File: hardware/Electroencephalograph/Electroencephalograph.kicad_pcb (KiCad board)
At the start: 2 copper layers, 89 parts, among them U1 ADS1298IPAG, U2 OPA330xxD

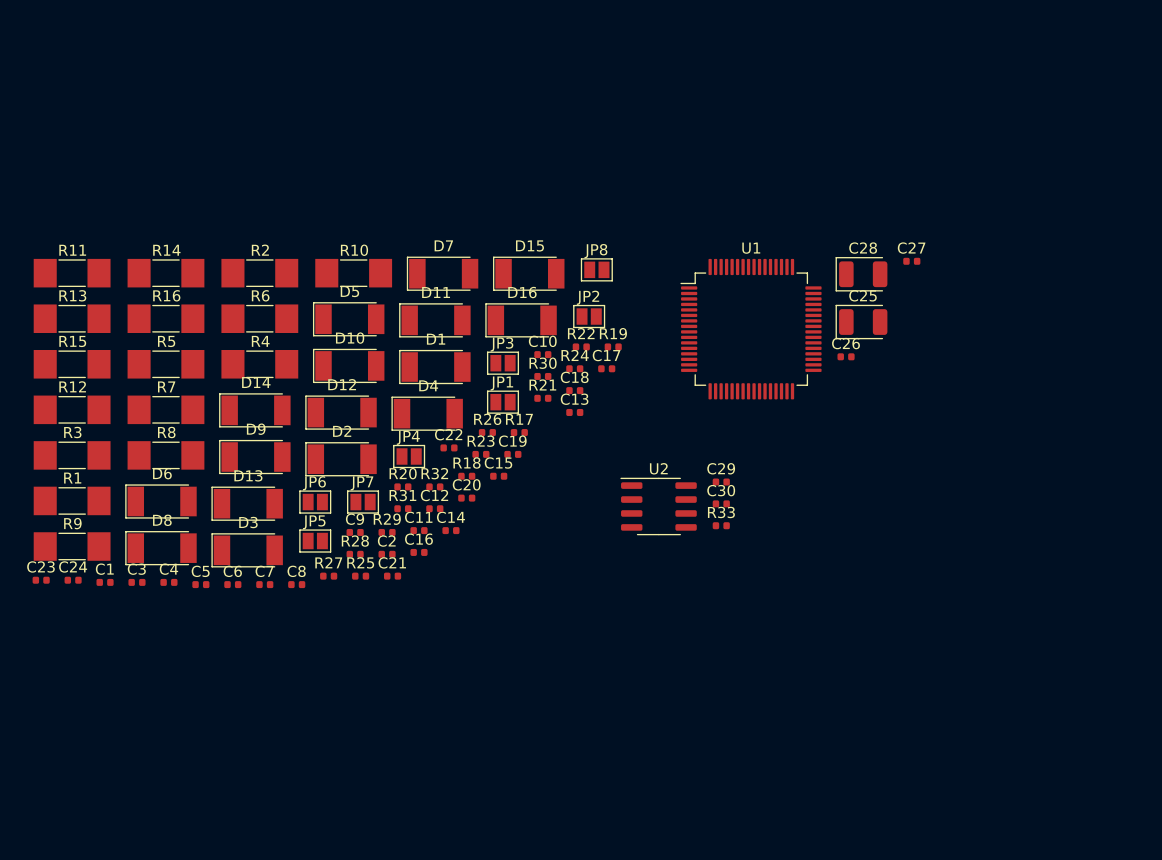
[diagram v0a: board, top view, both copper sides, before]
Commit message: paritial routing for analog part
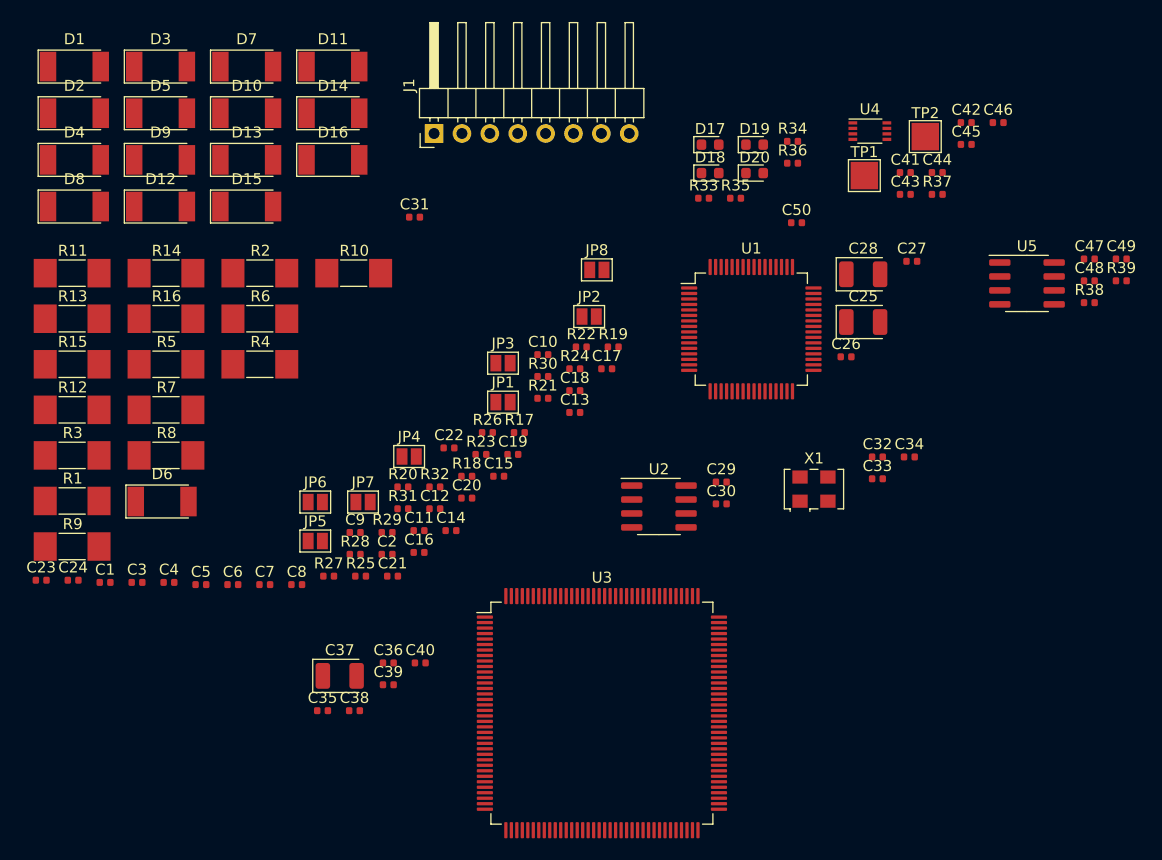
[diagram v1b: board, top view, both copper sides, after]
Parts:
- added C31: 1n, Capacitor_SMD:C_0402_1005Metric, F.Cu at (163.8, 45.0)
- added C32: 1u, Capacitor_SMD:C_0402_1005Metric, F.Cu at (206.0, 66.8)
- added C33: 1u, Capacitor_SMD:C_0402_1005Metric, F.Cu at (206.0, 68.8)
- added C34: 1u, Capacitor_SMD:C_0402_1005Metric, F.Cu at (208.9, 66.8)
- added C35: 100n, Capacitor_SMD:C_0402_1005Metric, F.Cu at (155.4, 89.9)
- added C36: 100n, Capacitor_SMD:C_0402_1005Metric, F.Cu at (161.4, 85.6)
- added C37: 10u, Capacitor_Tantalum_SMD:CP_EIA-3528-21_Kemet-B, F.Cu at (157.0, 86.7)
- added C38: 100n, Capacitor_SMD:C_0402_1005Metric, F.Cu at (158.4, 89.9)
- added C39: 1u, Capacitor_SMD:C_0402_1005Metric, F.Cu at (161.4, 87.6)
- added C40: 1u, Capacitor_SMD:C_0402_1005Metric, F.Cu at (164.3, 85.6)
- added C41: 1u, Capacitor_SMD:C_0402_1005Metric, F.Cu at (208.5, 40.9)
- added C42: 100n, Capacitor_SMD:C_0402_1005Metric, F.Cu at (214.1, 36.3)
- added C43: 100n, Capacitor_SMD:C_0402_1005Metric, F.Cu at (208.5, 42.9)
- added C44: 1u, Capacitor_SMD:C_0402_1005Metric, F.Cu at (211.4, 40.9)
- added C45: 10u, Capacitor_SMD:C_0402_1005Metric, F.Cu at (214.1, 38.3)
- added C46: 100u, Capacitor_SMD:C_0402_1005Metric, F.Cu at (217.0, 36.3)
- added C47: 100n, Capacitor_SMD:C_0402_1005Metric, F.Cu at (225.3, 48.8)
- added C48: 22n, Capacitor_SMD:C_0402_1005Metric, F.Cu at (225.3, 50.8)
- added C49: 100n, Capacitor_SMD:C_0402_1005Metric, F.Cu at (228.2, 48.8)
- added C50: 100n, Capacitor_SMD:C_0402_1005Metric, F.Cu at (198.6, 45.5)
- added D17: LED, LED_SMD:LED_0603_1608Metric, F.Cu at (190.8, 38.4)
- added D18: LED, LED_SMD:LED_0603_1608Metric, F.Cu at (190.8, 40.9)
- added D19: LED, LED_SMD:LED_0603_1608Metric, F.Cu at (194.8, 38.4)
- added D20: LED, LED_SMD:LED_0603_1608Metric, F.Cu at (194.8, 40.9)
- added J1: Conn_01x08_Male, Connector_PinHeader_2.54mm:PinHeader_1x08_P2.54mm_Horizontal, F.Cu at (165.6, 37.3)
- added R34: 220R, Resistor_SMD:R_0402_1005Metric, F.Cu at (198.3, 38.1)
- added R35: 220R, Resistor_SMD:R_0402_1005Metric, F.Cu at (193.1, 43.2)
- added R36: 220R, Resistor_SMD:R_0402_1005Metric, F.Cu at (198.3, 40.0)
- added R37: 100R, Resistor_SMD:R_0402_1005Metric, F.Cu at (211.4, 42.9)
- added R38: 10R, Resistor_SMD:R_0402_1005Metric, F.Cu at (225.3, 52.7)
- added R39: 100k, Resistor_SMD:R_0402_1005Metric, F.Cu at (228.2, 50.8)
- added TP1: TestPoint_Alt, TestPoint:TestPoint_Pad_2.5x2.5mm, F.Cu at (204.8, 41.2)
- added TP2: TestPoint_Alt, TestPoint:TestPoint_Pad_2.5x2.5mm, F.Cu at (210.4, 37.6)
- added U3: TMS320LF2406PZ, Package_QFP:LQFP-144_20x20mm_P0.5mm, F.Cu at (180.9, 90.1)
- added U4: REF5025, Package_SO:VSSOP-8_2.3x2mm_P0.5mm, F.Cu at (205.3, 37.1)
- added U5: OPA350, Package_SO:SOIC-8_3.9x4.9mm_P1.27mm, F.Cu at (219.6, 51.0)
- added X1: 2M048, Oscillator:Oscillator_SMD_EuroQuartz_XO53-4Pin_5.0x3.2mm, F.Cu at (200.2, 69.7)
- C25: value 1u -> 22u
- R33: value not mounted -> 220R
- moved D3 44.8 mm to (140.7, 31.2)
- moved D1 42.8 mm to (132.8, 31.2)
- moved D2 39.9 mm to (132.8, 35.5)
- moved D4 39.7 mm to (132.8, 39.7)
- moved D8 32.1 mm to (132.8, 44.0)
- moved D13 31.3 mm to (148.5, 39.7)
- moved R33 29.9 mm to (190.2, 43.2)
- moved D9 28.4 mm to (140.7, 39.7)
- moved D14 28.0 mm to (156.4, 35.5)
- moved D15 26.5 mm to (148.5, 44.0)
- moved D7 26.0 mm to (148.5, 31.2)
- moved D5 25.5 mm to (140.7, 35.5)
- moved D12 25.0 mm to (140.7, 44.0)
- moved D11 25.0 mm to (156.4, 31.2)
- moved D10 24.9 mm to (148.5, 35.5)
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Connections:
- C1 pad 1: Net-(C1-Pad1) -> ECC_1
- C2 pad 1: Net-(C2-Pad1) -> ECC_2
- C21 pad 1: Net-(C21-Pad1) -> ECC_6
- C22 pad 1: Net-(C22-Pad1) -> ECC_5
- C23 pad 1: Net-(C23-Pad1) -> ECC_8
- C24 pad 1: Net-(C24-Pad1) -> ECC_7
- C25 pad 2: GNDA -> VDDA
- C26 pad 1: Net-(C25-Pad1) -> Net-(C26-Pad1)
- C26 pad 2: GNDA -> VDDA
- C27 pad 1: Net-(C27-Pad1) -> VDDA
- C28 pad 1: Net-(C27-Pad1) -> VDDA
- C3 pad 1: Net-(C3-Pad1) -> ECC_4
- C4 pad 1: Net-(C4-Pad1) -> ECC_3
- D1 pad 1: Net-(C1-Pad2) -> VDDA
- D1 pad 2: VDDA -> Net-(C1-Pad2)
- D12 pad 1: VDDA -> Net-(C14-Pad1)
- D12 pad 2: Net-(C16-Pad1) -> VDDA
- D13 pad 1: Net-(C18-Pad1) -> VDDA
- D13 pad 2: VDDA -> Net-(C20-Pad1)
- D14 pad 2: Net-(C18-Pad1) -> Net-(D14-Pad2)
- D16 pad 1: VDDA -> Net-(D14-Pad2)
- D16 pad 2: Net-(C20-Pad1) -> VDDA
- D2 pad 2: Net-(C1-Pad2) -> Net-(C2-Pad2)
- D3 pad 1: Net-(C2-Pad2) -> Net-(C1-Pad2)
- D4 pad 1: VDDA -> Net-(C2-Pad2)
- D4 pad 2: Net-(C2-Pad2) -> VDDA
- D5 pad 1: Net-(C10-Pad1) -> VDDA
- D5 pad 2: VDDA -> Net-(C12-Pad1)
- D7 pad 1: Net-(C12-Pad1) -> Net-(C10-Pad1)
- D8 pad 1: VDDA -> Net-(C12-Pad1)
- D8 pad 2: Net-(C12-Pad1) -> VDDA
- D9 pad 1: Net-(C14-Pad1) -> VDDA
- D9 pad 2: VDDA -> Net-(C16-Pad1)
- JP1 pad 2: Net-(C1-Pad1) -> ECC_1
- JP2 pad 2: Net-(C2-Pad1) -> ECC_2
- JP3 pad 2: Net-(C3-Pad1) -> ECC_4
- JP4 pad 2: Net-(C4-Pad1) -> ECC_3
- JP5 pad 2: Net-(C21-Pad1) -> ECC_6
- JP6 pad 2: Net-(C22-Pad1) -> ECC_5
- JP7 pad 2: Net-(C23-Pad1) -> ECC_8
- JP8 pad 2: Net-(C24-Pad1) -> ECC_7
- R1 pad 2: (no net) -> /EEGFrontend/ELECTRODE_1
- R11 pad 2: (no net) -> /EEGFrontend/ELECTRODE_6
- R13 pad 2: (no net) -> /EEGFrontend/ELECTRODE_7
- R15 pad 2: (no net) -> /EEGFrontend/ELECTRODE_8
- R17 pad 1: Net-(C1-Pad1) -> ECC_1
- R18 pad 1: Net-(C2-Pad1) -> ECC_2
- R19 pad 1: GNDA -> VDDA
- R19 pad 2: Net-(C1-Pad1) -> ECC_1
- R20 pad 1: GNDA -> VDDA
- R20 pad 2: Net-(C2-Pad1) -> ECC_2
- R21 pad 1: Net-(C3-Pad1) -> ECC_4
- R22 pad 1: Net-(C4-Pad1) -> ECC_3
- R23 pad 1: GNDA -> VDDA
- R23 pad 2: Net-(C3-Pad1) -> ECC_4
- R24 pad 1: GNDA -> VDDA
- R24 pad 2: Net-(C4-Pad1) -> ECC_3
- R25 pad 1: Net-(C21-Pad1) -> ECC_6
- R26 pad 1: Net-(C22-Pad1) -> ECC_5
- R27 pad 1: GNDA -> VDDA
- R27 pad 2: Net-(C21-Pad1) -> ECC_6
- R28 pad 1: GNDA -> VDDA
- R28 pad 2: Net-(C22-Pad1) -> ECC_5
- R29 pad 1: Net-(C23-Pad1) -> ECC_8
- R3 pad 2: (no net) -> /EEGFrontend/ELECTRODE_2
- R30 pad 1: Net-(C24-Pad1) -> ECC_7
- R31 pad 1: GNDA -> VDDA
- R31 pad 2: Net-(C23-Pad1) -> ECC_8
- R32 pad 1: GNDA -> VDDA
- R32 pad 2: Net-(C24-Pad1) -> ECC_7
- R33 pad 1: (no net) -> Net-(D17-Pad2)
- R33 pad 2: (no net) -> Net-(R33-Pad2)
- R5 pad 2: (no net) -> /EEGFrontend/ELECTRODE_3
- R7 pad 2: (no net) -> /EEGFrontend/ELECTRODE_4
- R9 pad 2: (no net) -> /EEGFrontend/ELECTRODE_5
- U1 pad 1: Net-(U1-Pad1) -> Net-(C31-Pad1)
- U1 pad 10: (no net) -> ECC_4
- U1 pad 11: Net-(U1-Pad1) -> Net-(C31-Pad1)
- U1 pad 12: (no net) -> ECC_3
- U1 pad 13: Net-(U1-Pad1) -> Net-(C31-Pad1)
- U1 pad 14: (no net) -> ECC_2
- U1 pad 15: Net-(U1-Pad1) -> Net-(C31-Pad1)
- U1 pad 16: (no net) -> ECC_1
- U1 pad 17: (no net) -> Net-(TP1-Pad1)
- U1 pad 18: (no net) -> Net-(TP2-Pad1)
- U1 pad 19: (no net) -> VDDA
- U1 pad 2: (no net) -> ECC_8
- U1 pad 20: (no net) -> VDDA
- U1 pad 21: (no net) -> VDDA
- U1 pad 22: (no net) -> VDDA
- U1 pad 23: (no net) -> VDDA
- U1 pad 24: (no net) -> Net-(C37-Pad1)
- U1 pad 25: (no net) -> VDDA
- U1 pad 26: (no net) -> Net-(C33-Pad1)
- U1 pad 28: (no net) -> Net-(C25-Pad1)
- U1 pad 3: Net-(U1-Pad1) -> Net-(C31-Pad1)
- U1 pad 30: (no net) -> Net-(C34-Pad1)
- U1 pad 4: (no net) -> ECC_7
- U1 pad 41: (no net) -> GNDA
- U1 pad 42: (no net) -> Net-(R36-Pad2)
- U1 pad 44: (no net) -> Net-(R35-Pad2)
- U1 pad 45: (no net) -> Net-(R34-Pad2)
- U1 pad 46: (no net) -> Net-(R33-Pad2)
- U1 pad 48: (no net) -> VDDA
- U1 pad 5: Net-(U1-Pad1) -> Net-(C31-Pad1)
- U1 pad 50: Net-(C27-Pad1) -> VDDA
- U1 pad 54: Net-(C25-Pad1) -> (no net)
- U1 pad 55: (no net) -> Net-(C26-Pad1)
- U1 pad 56: Net-(C25-Pad1) -> VDDA
- U1 pad 57: GNDA -> VDDA
- U1 pad 58: GNDA -> VDDA
- U1 pad 59: Net-(C25-Pad1) -> VDDA
- U1 pad 6: (no net) -> ECC_6
- U1 pad 64: (no net) -> Net-(C31-Pad1)
- U1 pad 7: Net-(U1-Pad1) -> Net-(C31-Pad1)
- U1 pad 8: (no net) -> ECC_5
- U1 pad 9: Net-(U1-Pad1) -> Net-(C31-Pad1)

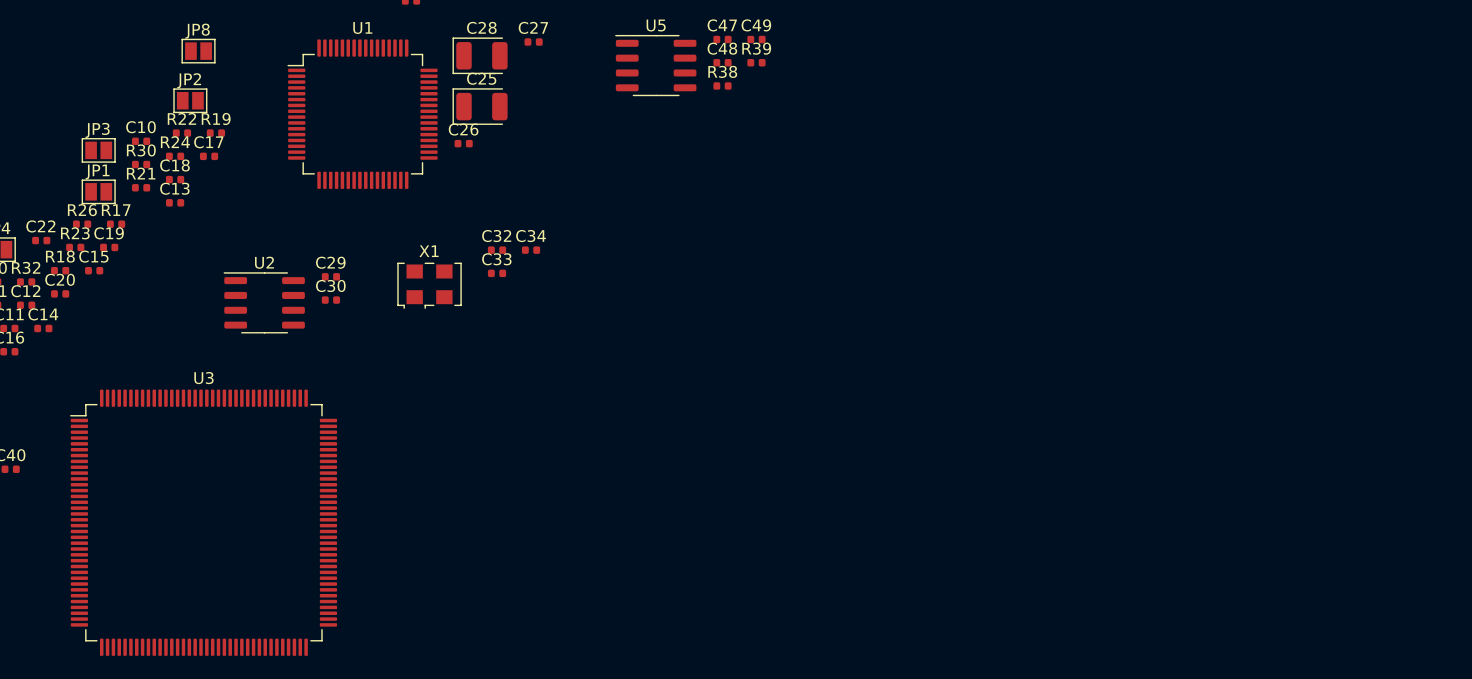
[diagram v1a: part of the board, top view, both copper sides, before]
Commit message: added spi isolator circuit
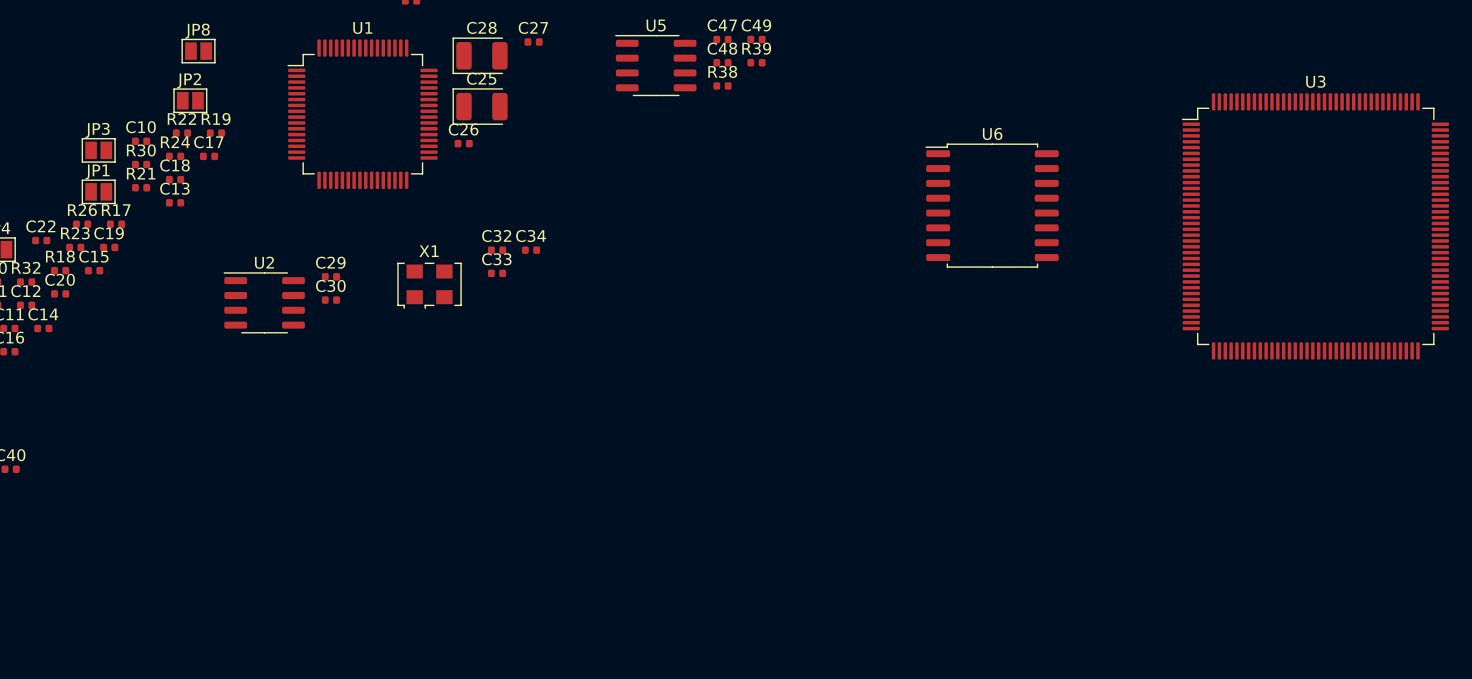
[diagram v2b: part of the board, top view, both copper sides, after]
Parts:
- added U6: ADUM2400, Package_SO:SOIC-16W_7.5x10.3mm_P1.27mm, F.Cu at (248.4, 63.0)
- moved U3 98.5 mm to (276.1, 64.8)
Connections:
- C37 pad 1: Net-(C37-Pad1) -> /EEGAcquisition/V_REF
- C38 pad 1: Net-(C37-Pad1) -> /EEGAcquisition/V_REF
- R38 pad 1: /EEGAcquisition/OSC -> /EEGAcquisition/V_REF
- R39 pad 1: /EEGAcquisition/OSC -> /EEGAcquisition/V_REF
- U1 pad 24: Net-(C37-Pad1) -> /EEGAcquisition/V_REF
- U1 pad 33: (no net) -> GNDA
- U1 pad 37: (no net) -> /EEGAcquisition/CLK
- X1 pad 3: (no net) -> /EEGAcquisition/CLK

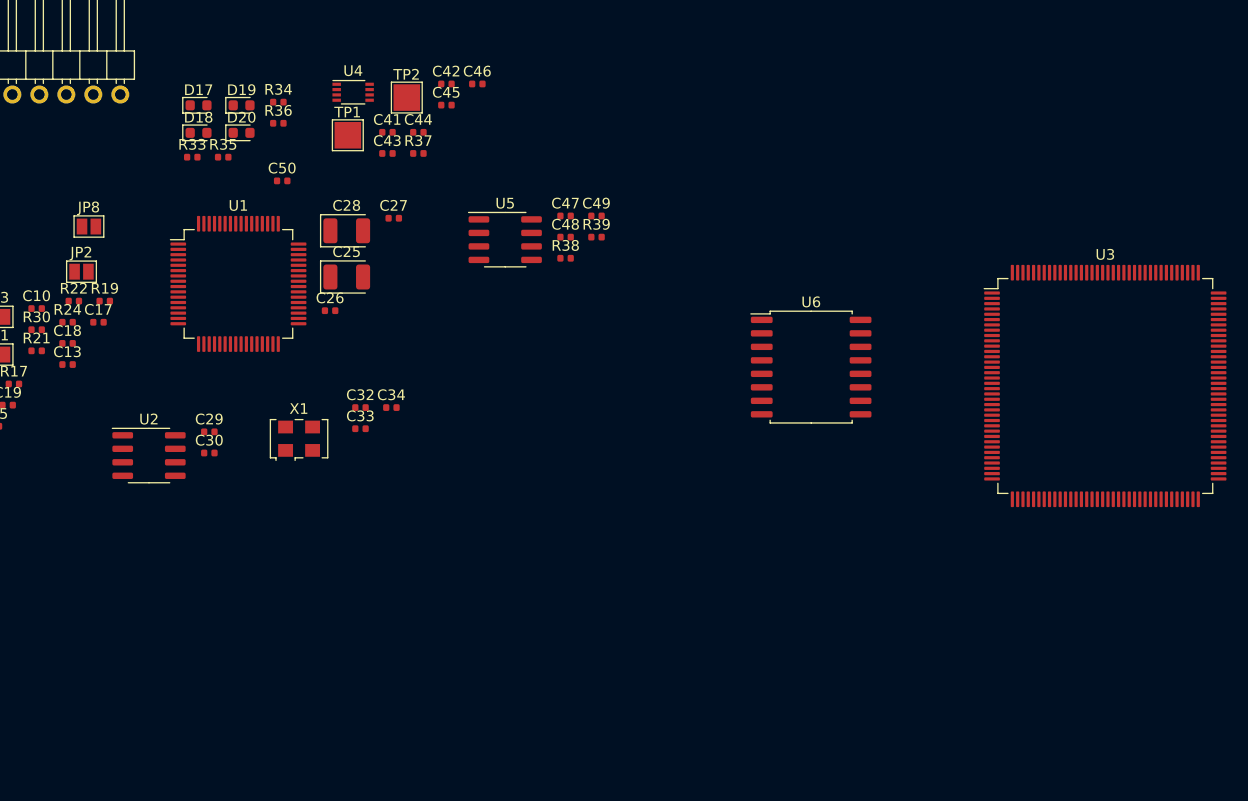
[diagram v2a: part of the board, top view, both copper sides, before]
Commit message: power circuit supply added
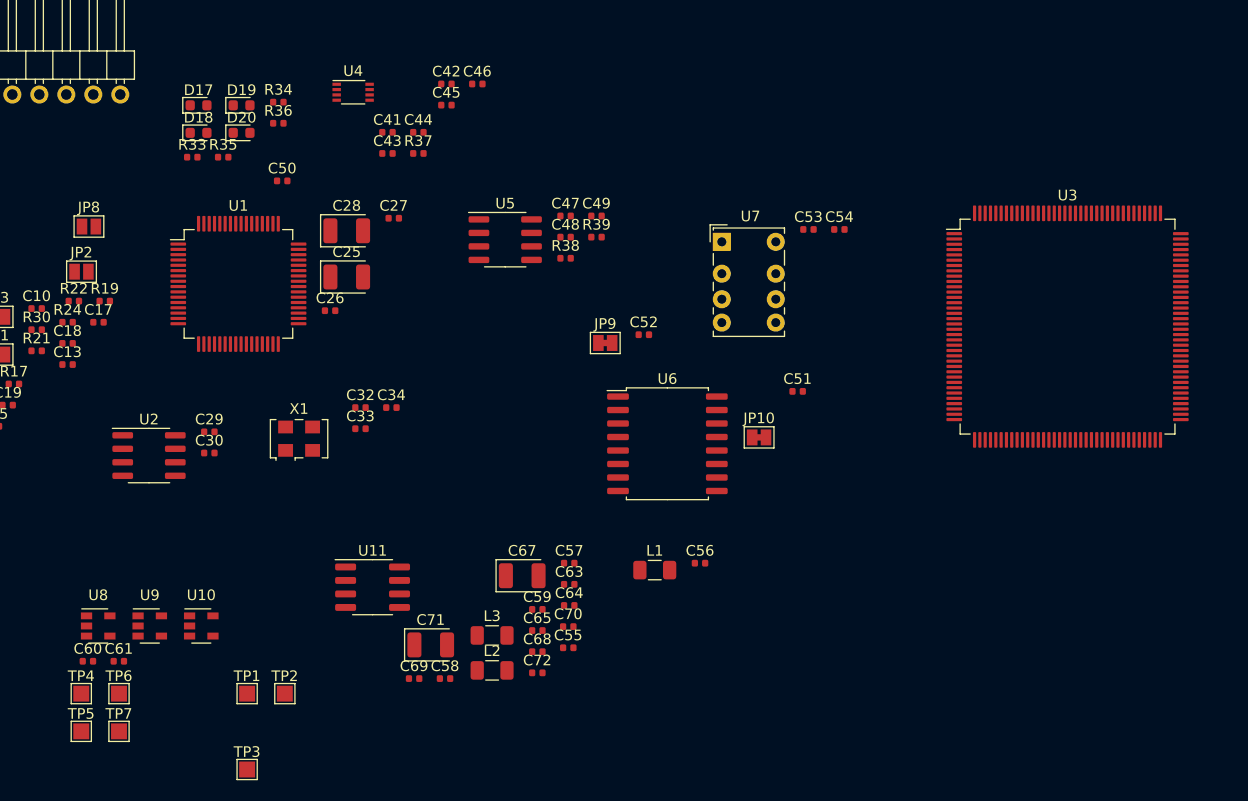
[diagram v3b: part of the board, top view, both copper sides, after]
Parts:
- added C51: 100n, Capacitor_SMD:C_0402_1005Metric, F.Cu at (247.1, 65.3)
- added C52: 100n, Capacitor_SMD:C_0402_1005Metric, F.Cu at (232.7, 59.9)
- added C53: 100n, Capacitor_SMD:C_0402_1005Metric, F.Cu at (248.2, 50.0)
- added C54: 100n, Capacitor_SMD:C_0402_1005Metric, F.Cu at (251.1, 50.0)
- added C55: 100n, Capacitor_SMD:C_0402_1005Metric, F.Cu at (225.6, 89.4)
- added C56: 100n, Capacitor_SMD:C_0402_1005Metric, F.Cu at (238.0, 81.4)
- added C57: 1u, Capacitor_SMD:C_0402_1005Metric, F.Cu at (225.6, 81.4)
- added C58: 100n, Capacitor_SMD:C_0402_1005Metric, F.Cu at (214.0, 92.3)
- added C59: 100n, Capacitor_SMD:C_0402_1005Metric, F.Cu at (222.6, 85.8)
- added C60: 1u, Capacitor_SMD:C_0402_1005Metric, F.Cu at (180.3, 90.7)
- added C61: 1u, Capacitor_SMD:C_0402_1005Metric, F.Cu at (183.2, 90.7)
- added C63: 1u, Capacitor_SMD:C_0402_1005Metric, F.Cu at (225.6, 83.4)
- added C64: 1u, Capacitor_SMD:C_0402_1005Metric, F.Cu at (225.6, 85.4)
- added C65: 1u, Capacitor_SMD:C_0402_1005Metric, F.Cu at (222.6, 87.8)
- added C67: 22u, Capacitor_Tantalum_SMD:CP_EIA-3528-21_Kemet-B, F.Cu at (221.2, 82.6)
- added C68: 1u, Capacitor_SMD:C_0402_1005Metric, F.Cu at (222.6, 89.8)
- added C69: 1u, Capacitor_SMD:C_0402_1005Metric, F.Cu at (211.0, 92.3)
- added C70: 1u, Capacitor_SMD:C_0402_1005Metric, F.Cu at (225.6, 87.4)
- added C71: 22u, Capacitor_Tantalum_SMD:CP_EIA-3528-21_Kemet-B, F.Cu at (212.6, 89.1)
- added C72: 1u, Capacitor_SMD:C_0402_1005Metric, F.Cu at (222.6, 91.8)
- added JP10: Jumper_NC_Small, Jumper:SolderJumper-2_P1.3mm_Bridged_Pad1.0x1.5mm, F.Cu at (243.5, 69.6)
- added JP9: Jumper_NC_Small, Jumper:SolderJumper-2_P1.3mm_Bridged_Pad1.0x1.5mm, F.Cu at (229.0, 60.7)
- added L1: 3u3, Inductor_SMD:L_1206_3216Metric, F.Cu at (233.7, 82.1)
- added L2: 3u3, Inductor_SMD:L_1206_3216Metric, F.Cu at (218.4, 91.5)
- added L3: 3u3, Inductor_SMD:L_1206_3216Metric, F.Cu at (218.4, 88.2)
- added TP3: TestPoint, TestPoint:TestPoint_Pad_1.5x1.5mm, F.Cu at (195.3, 100.9)
- added TP4: TestPoint, TestPoint:TestPoint_Pad_1.5x1.5mm, F.Cu at (179.7, 93.7)
- added TP5: TestPoint, TestPoint:TestPoint_Pad_1.5x1.5mm, F.Cu at (179.7, 97.3)
- added TP6: TestPoint, TestPoint:TestPoint_Pad_1.5x1.5mm, F.Cu at (183.3, 93.7)
- added TP7: TestPoint, TestPoint:TestPoint_Pad_1.5x1.5mm, F.Cu at (183.3, 97.3)
- added U10: TC1017-xCT, Package_TO_SOT_SMD:SOT-23-5, F.Cu at (191.0, 87.4)
- added U11: TPS60403, Package_SO:SOP-8_3.76x4.96mm_P1.27mm, F.Cu at (207.1, 83.7)
- added U7: THI3-0511, Relay_THT:Relay_DPDT_Omron_G6K-2P-Y, F.Cu at (240.0, 51.2)
- added U8: TC1017-xCT, Package_TO_SOT_SMD:SOT-23-5, F.Cu at (181.3, 87.4)
- added U9: TC1017-xCT, Package_TO_SOT_SMD:SOT-23-5, F.Cu at (186.2, 87.4)
- TP1, TP2: value TestPoint_Alt -> TestPoint; footprint TestPoint:TestPoint_Pad_2.5x2.5mm -> TestPoint:TestPoint_Pad_1.5x1.5mm
- U6: value ADUM2400 -> ADUM2401BRWZ
- moved TP2 57.3 mm to (198.9, 93.7)
- moved TP1 53.4 mm to (195.3, 93.7)
- moved U6 15.3 mm to (234.9, 70.2)
- moved U3 6.62 mm to (272.5, 59.2)
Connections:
- U6 pad 1: (no net) -> VDDA
- U6 pad 10: (no net) -> Net-(JP10-Pad1)
- U6 pad 15: (no net) -> GNDA
- U6 pad 16: (no net) -> VDDA
- U6 pad 2: (no net) -> GNDA
- U6 pad 7: (no net) -> Net-(JP9-Pad1)
- U6 pad 8: (no net) -> GNDA
- U6 pad 9: (no net) -> GNDA
